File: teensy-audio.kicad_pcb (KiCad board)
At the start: 2 copper layers, 80 x 140 mm, 49 parts, among them J1 AudioJack2, J10 Conn_01x05, J11 Conn_01x02, J12 Conn_01x04, J13 Conn_01x04, J2 AudioJack2, J3 Barrel_Jack, J4 Conn_02x06_Odd_Even, J5 Conn_02x08_Odd_Even, J6 Conn_02x05_Odd_Even, J7 Conn_01x04, J8 Conn_01x04, J9 Conn_02x05_Odd_Even, SW1 RotaryEncoder_Switch, SW2 SW_Push, SW3 SW_Push, SW4 SW_Push, SW5 SW_Push, U1 LM358, U2 LM7805_TO220, U3 Teensy4.0

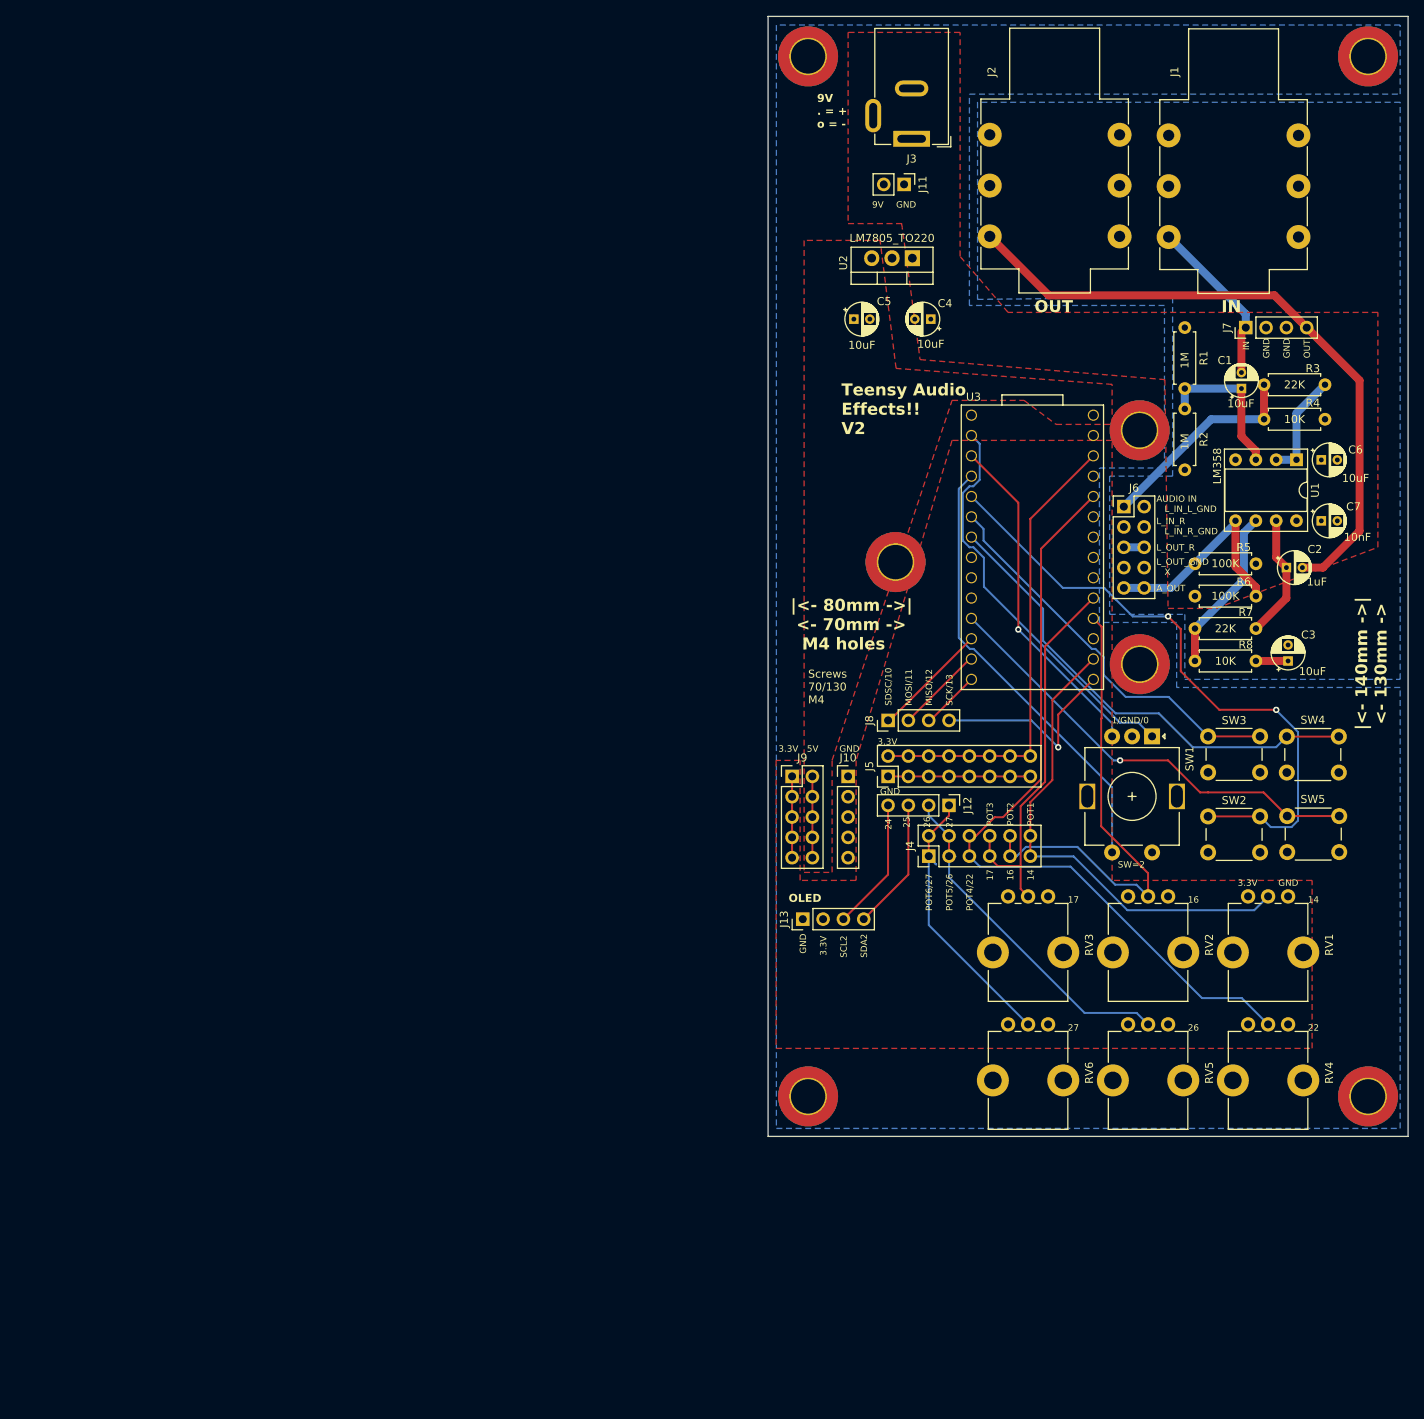
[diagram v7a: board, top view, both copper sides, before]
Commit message: stereo input and output
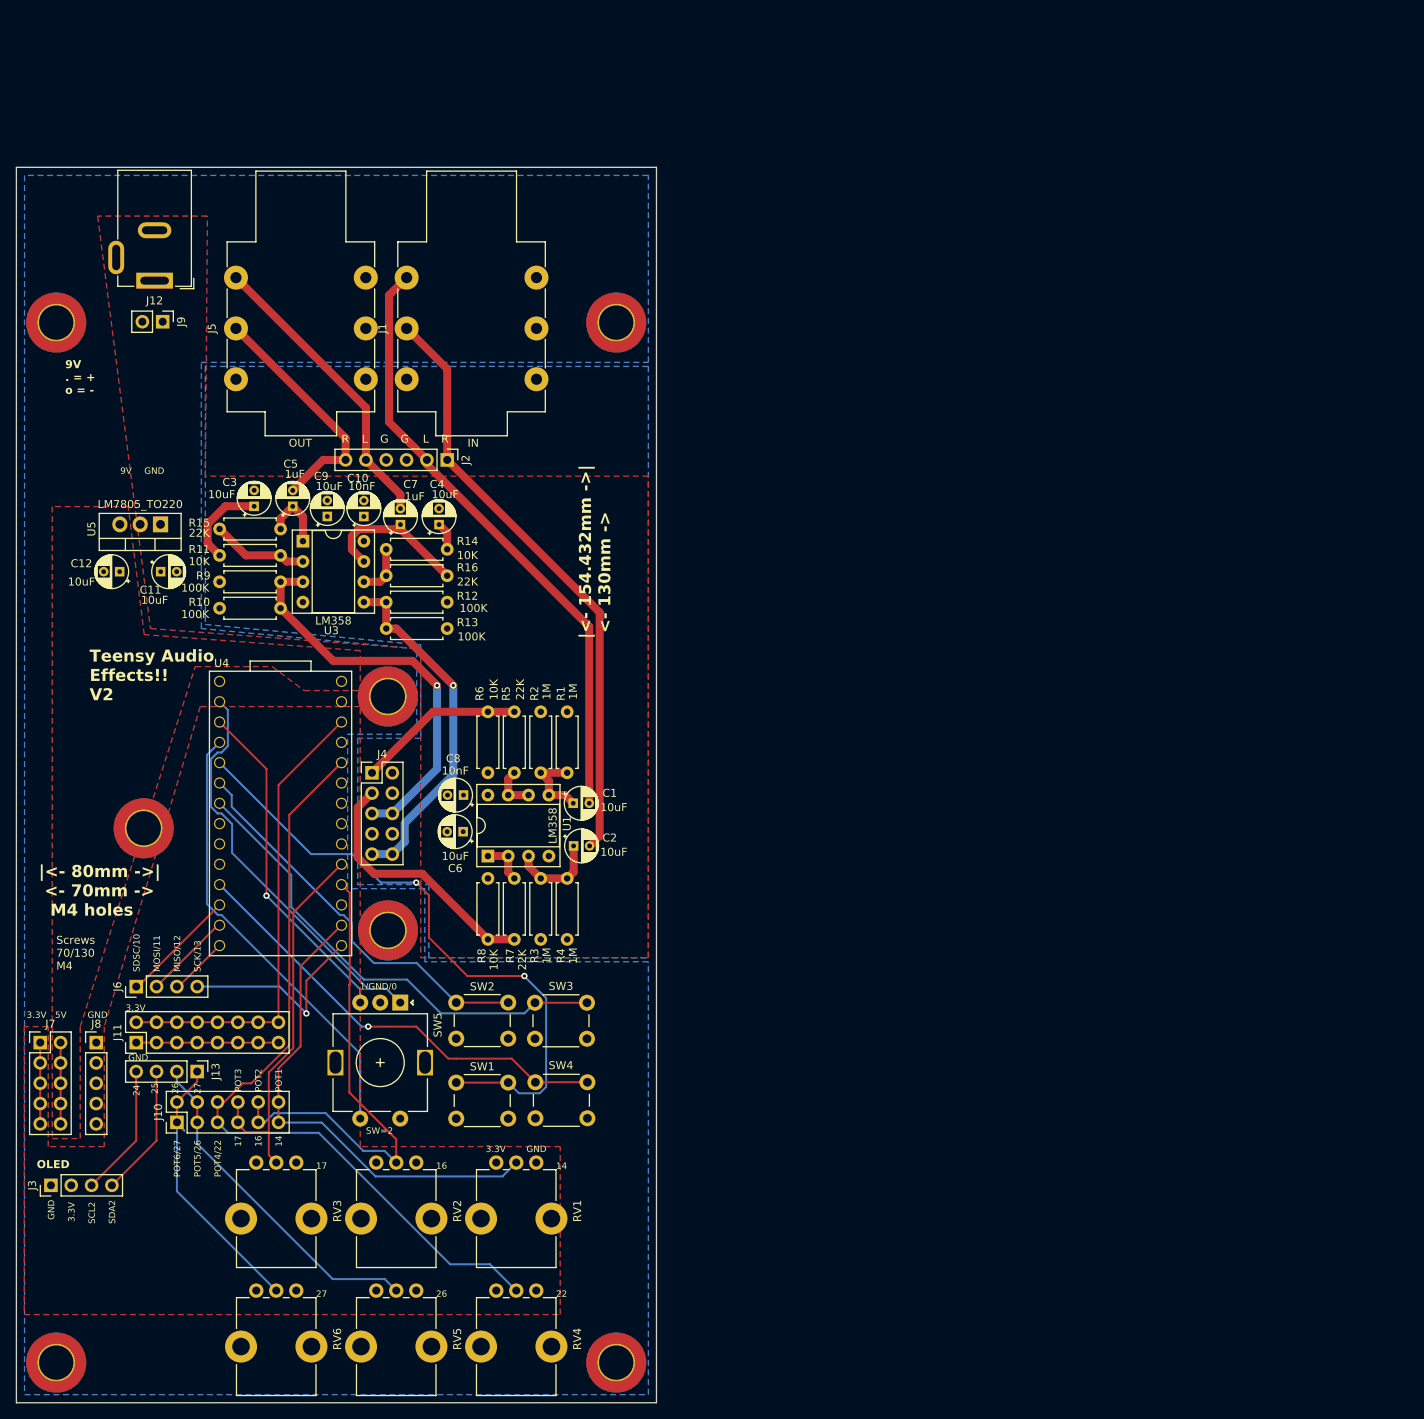
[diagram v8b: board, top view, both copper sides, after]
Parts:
- removed the J7 at (219.7, 58.9)
- added C1: 10uF, Capacitor_THT:CP_Radial_D4.0mm_P2.00mm, F.Cu at (135.6, 118.4)
- added C10: 10nF, Capacitor_THT:CP_Radial_D4.0mm_P2.00mm, F.Cu at (109.5, 82.5)
- added C4: 10uF, Capacitor_THT:CP_Radial_D4.0mm_P2.00mm, F.Cu at (118.9, 83.5)
- added C7: 1uF, Capacitor_THT:CP_Radial_D4.0mm_P2.00mm, F.Cu at (114.0, 83.5)
- added C9: 10uF, Capacitor_THT:CP_Radial_D4.0mm_P2.00mm, F.Cu at (104.9, 82.5)
- added J5: AudioJack3, Connector_Audio:Jack_6.35mm_Neutrik_NMJ6HFD2-AU_Horizontal, F.Cu at (93.5, 65.4)
- added R1: 1M, Resistor_THT:R_Axial_DIN0207_L6.3mm_D2.5mm_P7.62mm_Horizontal, F.Cu at (134.9, 106.9)
- added R12: 100K, Resistor_THT:R_Axial_DIN0207_L6.3mm_D2.5mm_P7.62mm_Horizontal, F.Cu at (119.9, 93.2)
- added R13: 100K, Resistor_THT:R_Axial_DIN0207_L6.3mm_D2.5mm_P7.62mm_Horizontal, F.Cu at (112.3, 96.5)
- added R14: 10K, Resistor_THT:R_Axial_DIN0207_L6.3mm_D2.5mm_P7.62mm_Horizontal, F.Cu at (112.3, 86.6)
- added R16: 22K, Resistor_THT:R_Axial_DIN0207_L6.3mm_D2.5mm_P7.62mm_Horizontal, F.Cu at (112.3, 89.9)
- added R2: 1M, Resistor_THT:R_Axial_DIN0207_L6.3mm_D2.5mm_P7.62mm_Horizontal, F.Cu at (131.6, 114.5)
- added R5: 22K, Resistor_THT:R_Axial_DIN0207_L6.3mm_D2.5mm_P7.62mm_Horizontal, F.Cu at (128.3, 114.5)
- added R6: 10K, Resistor_THT:R_Axial_DIN0207_L6.3mm_D2.5mm_P7.62mm_Horizontal, F.Cu at (125.0, 106.9)
- added U3: LM358, Package_DIP:DIP-8_W7.62mm_Socket, F.Cu at (101.9, 85.6)
- J1: value AudioJack2 -> AudioJack3
- J2: value AudioJack2 -> Conn_01x06; footprint Connector_Audio:Jack_6.35mm_Neutrik_NMJ6HFD2-AU_Horizontal -> Connector_PinHeader_2.54mm:PinHeader_1x06_P2.54mm_Vertical
- moved C3 130.7 mm to (95.8, 81.2)
- moved C5 124.4 mm to (100.6, 81.2), turned to 90 degrees
- moved R15 122.6 mm to (91.4, 84.1)
- moved R9 121.9 mm to (91.4, 90.7)
- moved R7 118.6 mm to (128.3, 127.8), turned to -90 degrees
- moved C6 116.9 mm to (121.9, 121.9), turned to 180 degrees
- moved R8 116.8 mm to (125.0, 135.4), turned to 90 degrees
- moved R11 115.1 mm to (99.1, 87.4), turned to 180 degrees
- moved R10 114.4 mm to (99.1, 94.0), turned to 180 degrees
- moved C8 112.6 mm to (121.9, 117.3), turned to 180 degrees
- moved U1 112.6 mm to (125.0, 125.0), turned to 90 degrees
- moved R3 111.0 mm to (131.6, 135.4), turned to 90 degrees
- moved C11 101.3 mm to (84.1, 89.4), turned to 0 degrees
- moved C2 101.2 mm to (135.7, 123.7), turned to 0 degrees
- moved SW4 99.7 mm to (137.4, 157.7)
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- renumbered C4 to C11, C5 to C12, C1 to C2, C2 to C5, C7 to C8, H4 to H2, H2 to H3, H5 to H4, H3 to H5, J4 to J10, J5 to J11, J3 to J12, J12 to J13, J13 to J3, J6 to J4, J8 to J6, J9 to J7, J10 to J8, J11 to J9, R5 to R10, R8 to R11, R7 to R15, R1 to R3, R2 to R4, R3 to R7, R4 to R8, R6 to R9, SW2 to SW1, SW3 to SW2, SW4 to SW3, SW5 to SW4, SW1 to SW5, U3 to U4, U2 to U5
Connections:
- net VREF renamed Net-(U1A-+)
- C2 pad 2: JACK_IN -> JACK_IN_R
- C5 pad 1: Net-(C2-Pad1) -> Net-(C5-Pad1)
- C5 pad 2: JACK_OUT -> JACK_OUT_R
- J1 pad R: (no net) -> JACK_IN_R
- J1 pad S: GNDA -> JACK_IN_L
- J1 pad T: JACK_IN -> GNDA
- J12 pad 3: GND -> (no net)
- J4 pad 1: AUDIO_IN -> LINE_IN_L
- J4 pad 10: AUDIO_OUT -> LINE_OUT_L
- J4 pad 9: AUDIO_OUT -> LINE_OUT_L
- R10 pad 1: AUDIO_OUT -> LINE_OUT_R
- R11 pad 1: Net-(U1B--) -> Net-(U3A--)
- R15 pad 1: Net-(U1B--) -> Net-(U3A--)
- R15 pad 2: Net-(C2-Pad1) -> Net-(C5-Pad1)
- R7 pad 2: AUDIO_IN -> LINE_IN_R
- R8 pad 1: AUDIO_IN -> LINE_IN_R
- R9 pad 2: AUDIO_OUT -> LINE_OUT_R
- U1 pad 5: AUDIO_OUT -> Net-(U1B-+)
- U1 pad 7: Net-(C2-Pad1) -> Net-(U1B--)
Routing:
- net JACK_OUT: track 81.5 -> 0.00 mm
- net JACK_IN_L: track 0.00 -> 77.2 mm
- net JACK_IN_R: track 0.00 -> 75.2 mm
- net LINE_OUT_R: track 2.54 -> 50.5 mm, vias 0 -> 1
- net LINE_OUT_L: track 0.00 -> 44.2 mm, vias 0 -> 1
- net JACK_OUT_L: track 0.00 -> 37.4 mm
- net LINE_IN_R: track 0.00 -> 32.6 mm
- net JACK_OUT_R: track 0.00 -> 30.3 mm
- net AUDIO_OUT: track 28.1 -> 0.00 mm
- net AUDIO_IN: track 26.4 -> 0.00 mm
- net JACK_IN: track 21.2 -> 0.00 mm
- net LINE_IN_L: track 0.00 -> 21.0 mm
- net Net-(C7-Pad1): track 0.00 -> 19.3 mm
- net Net-(C2-Pad1): track 15.6 -> 0.00 mm
- net Net-(U1B--): track 20.7 -> 5.65 mm
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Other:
- board size 80 x 140 mm -> 80 x 154.4 mm
- board text added: "G"
- board text added: "L"
- board text added: "R"
- board text added: "|<- 154.432mm ->| <- 130mm ->"
- board text removed: "AUDIO IN"
- board text removed: "A_OUT"
- board text removed: "L_IN_L_GND"
- board text removed: "L_IN_R"
- board text removed: "L_IN_R_GND"
- board text removed: "L_OUT_GND"
- board text removed: "L_OUT_R"
- board text removed: "X"
- board text removed: "|<- 140mm ->| <- 130mm ->"
